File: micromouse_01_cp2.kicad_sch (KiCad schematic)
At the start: 26 parts, among them IC1 MPU-6500, IC2 DRV8835DSSR, M1 MK06-4.5, M2 MK06-4.5, U1 MA730, U12 ESP32-S3-MINI-1-N8, U2 MA730

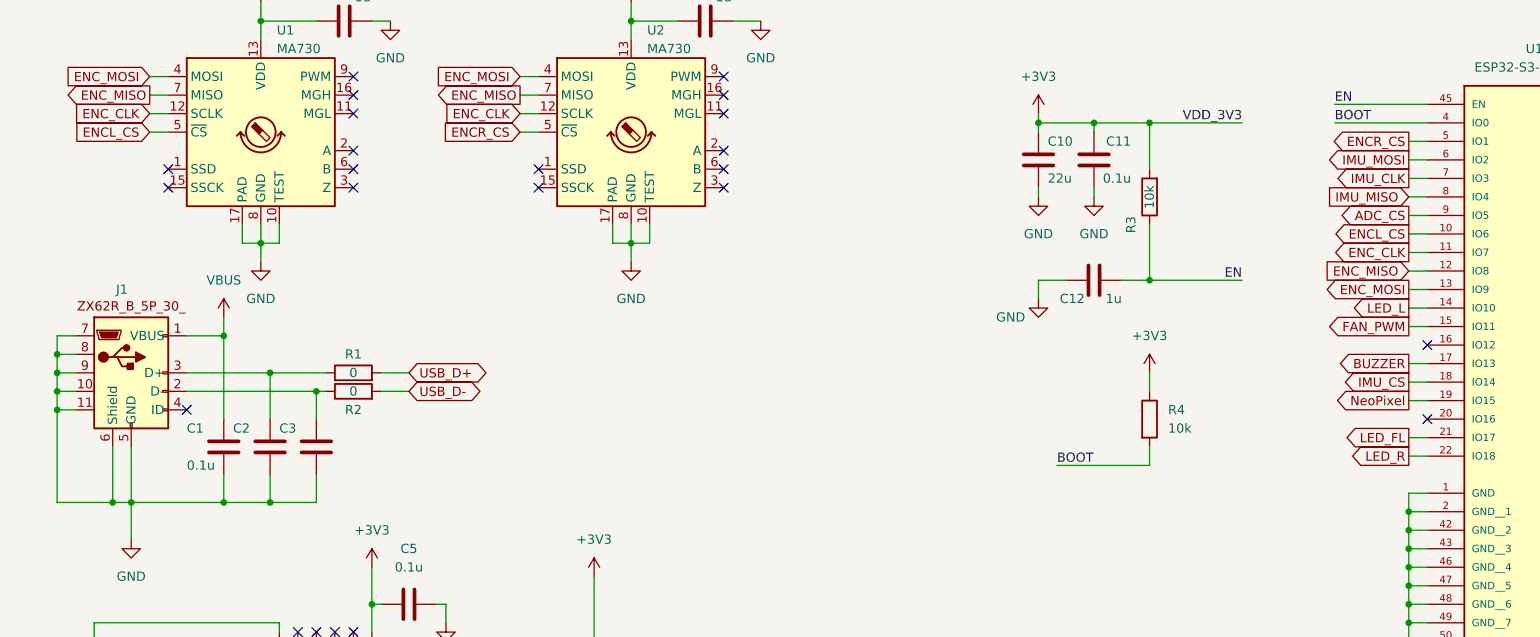
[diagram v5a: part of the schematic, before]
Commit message: 回路図完成 PCB配線途中
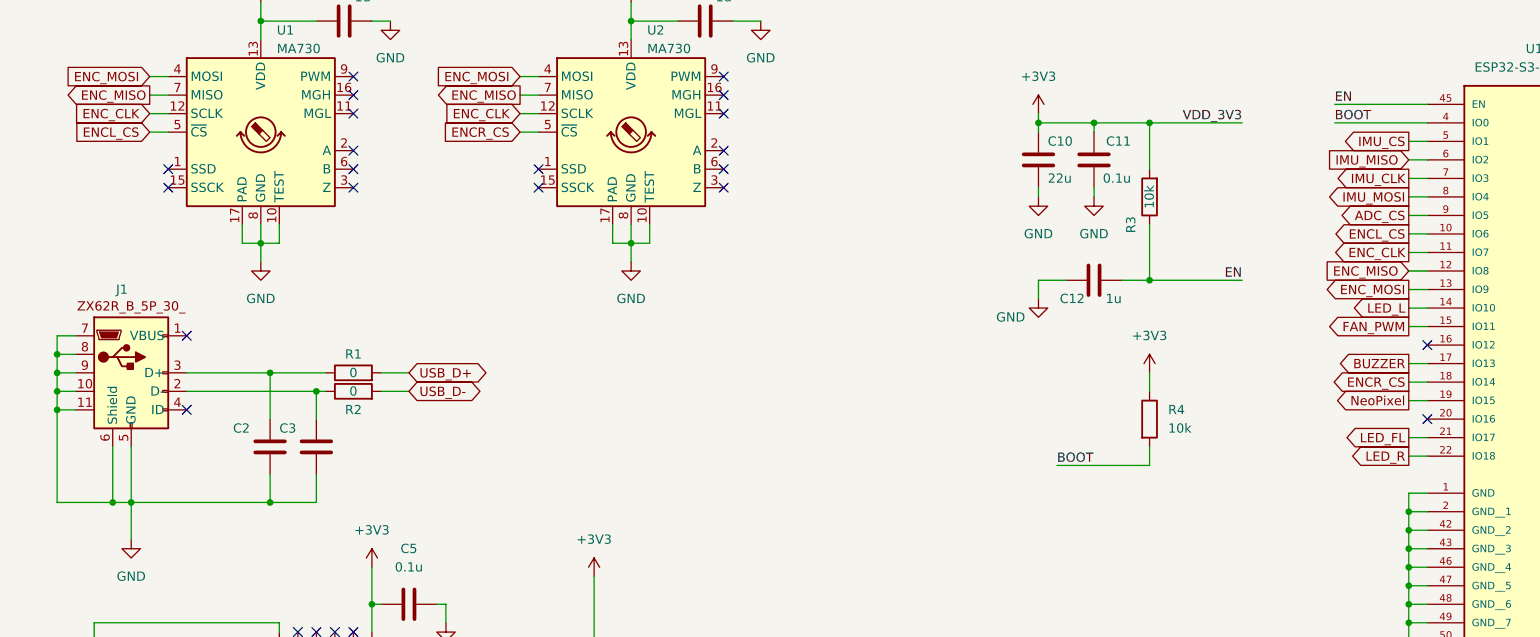
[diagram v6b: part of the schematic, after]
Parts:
- removed C1: 0.1u, Capacitor_SMD:C_0402_1005Metric, symbol Device:C
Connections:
- net ENCR_CS: now also U12.18 (IO14); no longer U12.5 (IO1)
- net IMU_CS: now also U12.5 (IO1); no longer U12.18 (IO14)
- net IMU_MISO: now also U12.6 (IO2); no longer U12.8 (IO4)
- net IMU_MOSI: now also U12.8 (IO4); no longer U12.6 (IO2)
- net VBUS: no longer names the net of J1.1 (VBUS)
- no-connect marks 43 -> 44
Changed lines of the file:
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@@
   (junction (at 252.73 102.87) (diameter 0) (color 0 0 0 0)
   )
-  (junction (at 53.34 88.9) (diameter 0) (color 0 0 0 0)
-  )
   (junction (at 38.1 88.9) (diameter 0) (color 0 0 0 0)
   )
@@
   )
   (junction (at 252.73 92.71) (diameter 0) (color 0 0 0 0)
-  )
-  (junction (at 53.34 66.04) (diameter 0) (color 0 0 0 0)
   )
   (junction (at 252.73 97.79) (diameter 0) (color 0 0 0 0)
@@
   (no_connect (at 63.5 137.16))
   (no_connect (at 38.1 119.38))
+  (no_connect (at 48.26 66.04))
   (no_connect (at 248.92 36.83))
   (no_connect (at 48.26 76.2))
@@
     (stroke (width 0) (type default))
   )
-  (wire (pts (xy 48.26 66.04) (xy 53.34 66.04))
-    (stroke (width 0) (type default))
-  )
   (wire (pts (xy 248.92 120.65) (xy 252.73 120.65))
     (stroke (width 0) (type default))
@@
     (stroke (width 0) (type default))
   )
-  (wire (pts (xy 40.64 88.9) (xy 53.34 88.9))
+  (wire (pts (xy 40.64 88.9) (xy 59.69 88.9))
     (stroke (width 0) (type default))
   )
@@
     (stroke (width 0) (type default))
   )
-  (wire (pts (xy 53.34 66.04) (xy 53.34 63.5))
-    (stroke (width 0) (type default))
-  )
-  (wire (pts (xy 53.34 88.9) (xy 59.69 88.9))
-    (stroke (width 0) (type default))
-  )
   (wire (pts (xy 57.15 177.8) (xy 74.93 177.8))
     (stroke (width 0) (type default))
@@
     (stroke (width 0) (type default))
   )
-  (wire (pts (xy 53.34 85.09) (xy 53.34 88.9))
-    (stroke (width 0) (type default))
-  )
   (wire (pts (xy 143.51 156.21) (xy 143.51 158.75))
     (stroke (width 0) (type default))
@@
   )
   (wire (pts (xy 99.06 127) (xy 104.14 127))
-    (stroke (width 0) (type default))
-  )
-  (wire (pts (xy 53.34 77.47) (xy 53.34 66.04))
     (stroke (width 0) (type default))
   )
@@
     (effects (font (size 1.27 1.27)) (justify right))
     (property "Intersheetrefs" "${INTERSHEET_REFS}" (at 81.6815 30.48 0)
+      (effects (font (size 1.27 1.27)) (justify right) hide)
+    )
+  )
+  (global_label "IMU_CS" (shape output) (at 215.9 39.37 180) (fields_autoplaced)
+    (effects (font (size 1.27 1.27)) (justify right))
+    (property "Intersheetrefs" "${INTERSHEET_REFS}" (at 206.081 39.37 0)
       (effects (font (size 1.27 1.27)) (justify right) hide)
     )
@@
     )
   )
-  (global_label "IMU_CS" (shape output) (at 215.9 72.39 180) (fields_autoplaced)
-    (effects (font (size 1.27 1.27)) (justify right))
-    (property "Intersheetrefs" "${INTERSHEET_REFS}" (at 206.081 72.39 0)
+  (global_label "IMU_MOSI" (shape output) (at 215.9 46.99 180) (fields_autoplaced)
+    (effects (font (size 1.27 1.27)) (justify right))
+    (property "Intersheetrefs" "${INTERSHEET_REFS}" (at 203.9643 46.99 0)
       (effects (font (size 1.27 1.27)) (justify right) hide)
     )
@@
     )
   )
+  (global_label "IMU_CLK" (shape output) (at 215.9 44.45 180) (fields_autoplaced)
+    (effects (font (size 1.27 1.27)) (justify right))
+    (property "Intersheetrefs" "${INTERSHEET_REFS}" (at 204.9924 44.45 0)
+      (effects (font (size 1.27 1.27)) (justify right) hide)
+    )
+  )
   (global_label "MOT2_ENBL" (shape output) (at 251.46 80.01 0) (fields_autoplaced)
     (effects (font (size 1.27 1.27)) (justify left))
@@
     )
   )
-  (global_label "ENCR_CS" (shape output) (at 215.9 39.37 180) (fields_autoplaced)
-    (effects (font (size 1.27 1.27)) (justify right))
-    (property "Intersheetrefs" "${INTERSHEET_REFS}" (at 204.4482 39.37 0)
-      (effects (font (size 1.27 1.27)) (justify right) hide)
-    )
-  )
   (global_label "IMU_MISO" (shape output) (at 106.68 115.57 0) (fields_autoplaced)
     (effects (font (size 1.27 1.27)) (justify left))
@@
     )
   )
+  (global_label "IMU_MISO" (shape input) (at 215.9 41.91 180) (fields_autoplaced)
+    (effects (font (size 1.27 1.27)) (justify right))
+    (property "Intersheetrefs" "${INTERSHEET_REFS}" (at 203.9643 41.91 0)
+      (effects (font (size 1.27 1.27)) (justify right) hide)
+    )
+  )
   (global_label "MOT1_ENBL" (shape input) (at 130.81 170.18 0) (fields_autoplaced)
     (effects (font (size 1.27 1.27)) (justify left))
@@
     )
   )
-  (global_label "IMU_MISO" (shape input) (at 215.9 46.99 180) (fields_autoplaced)
-    (effects (font (size 1.27 1.27)) (justify right))
-    (property "Intersheetrefs" "${INTERSHEET_REFS}" (at 203.9643 46.99 0)
-      (effects (font (size 1.27 1.27)) (justify right) hide)
-    )
-  )
-  (global_label "IMU_CLK" (shape output) (at 215.9 44.45 180) (fields_autoplaced)
-    (effects (font (size 1.27 1.27)) (justify right))
-    (property "Intersheetrefs" "${INTERSHEET_REFS}" (at 204.9924 44.45 0)
-      (effects (font (size 1.27 1.27)) (justify right) hide)
-    )
-  )
   (global_label "ENC_MISO" (shape output) (at 43.18 33.02 180) (fields_autoplaced)
     (effects (font (size 1.27 1.27)) (justify right))
@@
     )
   )
+  (global_label "ENCR_CS" (shape output) (at 215.9 72.39 180) (fields_autoplaced)
+    (effects (font (size 1.27 1.27)) (justify right))
+    (property "Intersheetrefs" "${INTERSHEET_REFS}" (at 204.4482 72.39 0)
+      (effects (font (size 1.27 1.27)) (justify right) hide)
+    )
+  )
   (global_label "ENC_MISO" (shape output) (at 93.98 33.02 180) (fields_autoplaced)
     (effects (font (size 1.27 1.27)) (justify right))
@@
     (effects (font (size 1.27 1.27)) (justify right))
     (property "Intersheetrefs" "${INTERSHEET_REFS}" (at 204.6296 54.61 0)
-      (effects (font (size 1.27 1.27)) (justify right) hide)
-    )
-  )
-  (global_label "IMU_MOSI" (shape output) (at 215.9 41.91 180) (fields_autoplaced)
-    (effects (font (size 1.27 1.27)) (justify right))
-    (property "Intersheetrefs" "${INTERSHEET_REFS}" (at 203.9643 41.91 0)
       (effects (font (size 1.27 1.27)) (justify right) hide)
     )
@@
         )
       )
-    )
-  )
-  (symbol (lib_id "Device:C") (at 53.34 81.28 0) (unit 1)
-    (in_bom yes) (on_board yes) (dnp no)
-    (property "Reference" "C1" (at 48.26 78.74 0)
-      (effects (font (size 1.27 1.27)) (justify left))
-    )
-    (property "Value" "0.1u" (at 48.26 83.82 0)
-      (effects (font (size 1.27 1.27)) (justify left))
-    )
-    (property "Footprint" "Capacitor_SMD:C_0402_1005Metric" (at 54.3052 85.09 0)
-      (effects (font (size 1.27 1.27)) hide)
-    )
-    (property "Datasheet" "~" (at 53.34 81.28 0)
-      (effects (font (size 1.27 1.27)) hide)
-    )
-    (pin "1")
-    (pin "2")
-    (instances
-      (project "micromouse_01_cp2"
-        (path "/619a00a9-cfa2-4255-85f4-bd5efe9f55d3"
-          (reference "C1") (unit 1)
-        )
-      )
-    )
-  )
-  (symbol (lib_id "power:VBUS") (at 53.34 63.5 0) (unit 1)
-    (in_bom yes) (on_board yes) (dnp no) (fields_autoplaced)
-    (property "Reference" "#PWR03" (at 53.34 67.31 0)
-      (effects (font (size 1.27 1.27)) hide)
-    )
-    (property "Value" "VBUS" (at 53.34 58.42 0)
-      (effects (font (size 1.27 1.27)))
-    )
-    (property "Footprint" "" (at 53.34 63.5 0)
-      (effects (font (size 1.27 1.27)) hide)
-    )
-    (property "Datasheet" "" (at 53.34 63.5 0)
-      (effects (font (size 1.27 1.27)) hide)
-    )
-    (pin "1")
-    (instances
-      (project "micromouse_01_cp2"
-        (path "/619a00a9-cfa2-4255-85f4-bd5efe9f55d3"
-          (reference "#PWR03") (unit 1)
-        )
-      )

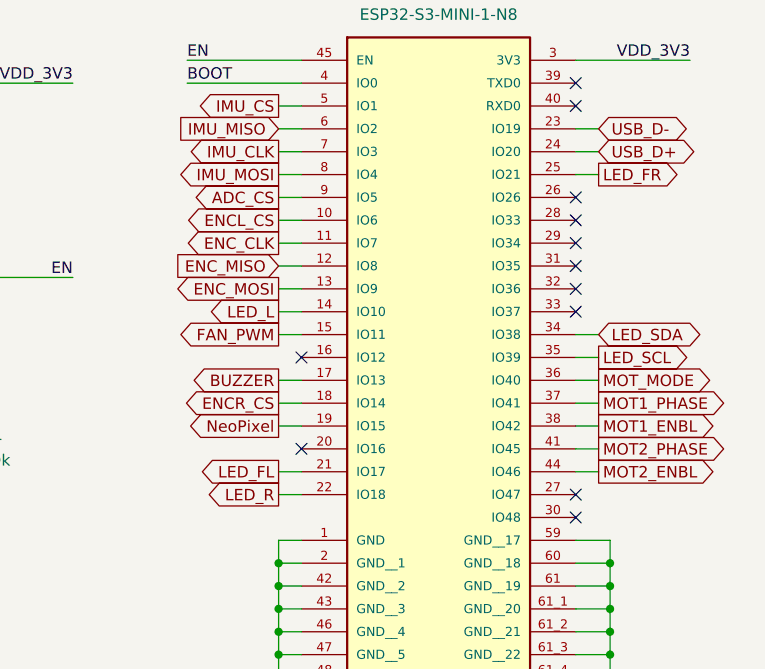
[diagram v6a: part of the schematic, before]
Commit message: Added 3D model
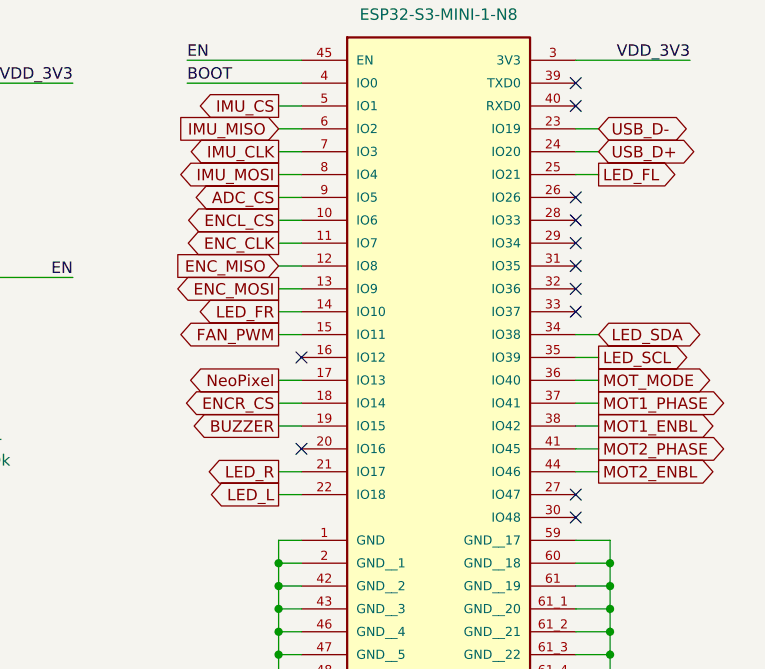
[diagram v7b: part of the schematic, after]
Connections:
- net BUZZER: now also U12.19 (IO15); no longer U12.17 (IO13)
- net LED_FL: now also U12.25 (IO21); no longer U12.21 (IO17)
- net LED_FR: now also U12.14 (IO10); no longer U12.25 (IO21)
- net LED_L: now also U12.22 (IO18); no longer U12.14 (IO10)
- net LED_R: now also U12.21 (IO17); no longer U12.22 (IO18)
- net NeoPixel: now also U12.17 (IO13); no longer U12.19 (IO15)
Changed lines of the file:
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@@
-    )
-  )
-  (global_label "NeoPixel" (shape output) (at 215.9 74.93 180) (fields_autoplaced)
-    (effects (font (size 1.27 1.27)) (justify right))
-    (property "Intersheetrefs" "${INTERSHEET_REFS}" (at 204.69 74.93 0)
-      (effects (font (size 1.27 1.27)) (justify right) hide)
     )
   )
@@
     )
   )
-  (global_label "LED_FR" (shape output) (at 251.46 46.99 0) (fields_autoplaced)
-    (effects (font (size 1.27 1.27)) (justify left))
-    (property "Intersheetrefs" "${INTERSHEET_REFS}" (at 261.2185 46.99 0)
-      (effects (font (size 1.27 1.27)) (justify left) hide)
-    )
-  )
   (global_label "IMU_MOSI" (shape output) (at 215.9 46.99 180) (fields_autoplaced)
     (effects (font (size 1.27 1.27)) (justify right))
@@
     )
   )
+  (global_label "BUZZER" (shape output) (at 215.9 74.93 180) (fields_autoplaced)
+    (effects (font (size 1.27 1.27)) (justify right))
+    (property "Intersheetrefs" "${INTERSHEET_REFS}" (at 205.4763 74.93 0)
+      (effects (font (size 1.27 1.27)) (justify right) hide)
+    )
+  )
   (global_label "LED_SCL" (shape output) (at 251.46 67.31 0) (fields_autoplaced)
     (effects (font (size 1.27 1.27)) (justify left))
@@
     )
   )
-  (global_label "LED_R" (shape output) (at 215.9 82.55 180) (fields_autoplaced)
-    (effects (font (size 1.27 1.27)) (justify right))
-    (property "Intersheetrefs" "${INTERSHEET_REFS}" (at 207.2301 82.55 0)
-      (effects (font (size 1.27 1.27)) (justify right) hide)
-    )
-  )
   (global_label "IMU_CLK" (shape input) (at 31.75 124.46 180) (fields_autoplaced)
     (effects (font (size 1.27 1.27)) (justify right))
@@
     )
   )
-  (global_label "LED_L" (shape output) (at 215.9 62.23 180) (fields_autoplaced)
-    (effects (font (size 1.27 1.27)) (justify right))
-    (property "Intersheetrefs" "${INTERSHEET_REFS}" (at 207.472 62.23 0)
+  (global_label "LED_FR" (shape output) (at 215.9 62.23 180) (fields_autoplaced)
+    (effects (font (size 1.27 1.27)) (justify right))
+    (property "Intersheetrefs" "${INTERSHEET_REFS}" (at 206.1415 62.23 0)
       (effects (font (size 1.27 1.27)) (justify right) hide)
     )
@@
     )
   )
+  (global_label "LED_FL" (shape output) (at 251.46 46.99 0) (fields_autoplaced)
+    (effects (font (size 1.27 1.27)) (justify left))
+    (property "Intersheetrefs" "${INTERSHEET_REFS}" (at 260.9766 46.99 0)
+      (effects (font (size 1.27 1.27)) (justify left) hide)
+    )
+  )
   (global_label "ENC_CLK" (shape input) (at 93.98 35.56 180) (fields_autoplaced)
     (effects (font (size 1.27 1.27)) (justify right))
@@
     )
   )
+  (global_label "NeoPixel" (shape output) (at 215.9 69.85 180) (fields_autoplaced)
+    (effects (font (size 1.27 1.27)) (justify right))
+    (property "Intersheetrefs" "${INTERSHEET_REFS}" (at 204.69 69.85 0)
+      (effects (font (size 1.27 1.27)) (justify right) hide)
+    )
+  )
   (global_label "MOT1_PHASE" (shape input) (at 130.81 172.72 0) (fields_autoplaced)
     (effects (font (size 1.27 1.27)) (justify left))
@@
     )
   )
+  (global_label "LED_R" (shape output) (at 215.9 80.01 180) (fields_autoplaced)
+    (effects (font (size 1.27 1.27)) (justify right))
+    (property "Intersheetrefs" "${INTERSHEET_REFS}" (at 207.2301 80.01 0)
+      (effects (font (size 1.27 1.27)) (justify right) hide)
+    )
+  )
   (global_label "MOT_MODE" (shape output) (at 251.46 69.85 0) (fields_autoplaced)
     (effects (font (size 1.27 1.27)) (justify left))
@@
     )
   )
-  (global_label "LED_FL" (shape output) (at 215.9 80.01 180) (fields_autoplaced)
-    (effects (font (size 1.27 1.27)) (justify right))
-    (property "Intersheetrefs" "${INTERSHEET_REFS}" (at 206.3834 80.01 0)
-      (effects (font (size 1.27 1.27)) (justify right) hide)
-    )
-  )
-  (global_label "BUZZER" (shape output) (at 215.9 69.85 180) (fields_autoplaced)
-    (effects (font (size 1.27 1.27)) (justify right))
-    (property "Intersheetrefs" "${INTERSHEET_REFS}" (at 205.4763 69.85 0)
-      (effects (font (size 1.27 1.27)) (justify right) hide)
-    )
+  (global_label "LED_L" (shape output) (at 215.9 82.55 180) (fields_autoplaced)
+    (effects (font (size 1.27 1.27)) (justify right))
+    (property "Intersheetrefs" "${INTERSHEET_REFS}" (at 207.472 82.55 0)
+      (effects (font (size 1.27 1.27)) (justify right) hide)
+    )
